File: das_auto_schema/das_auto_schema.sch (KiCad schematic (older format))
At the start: 0 parts

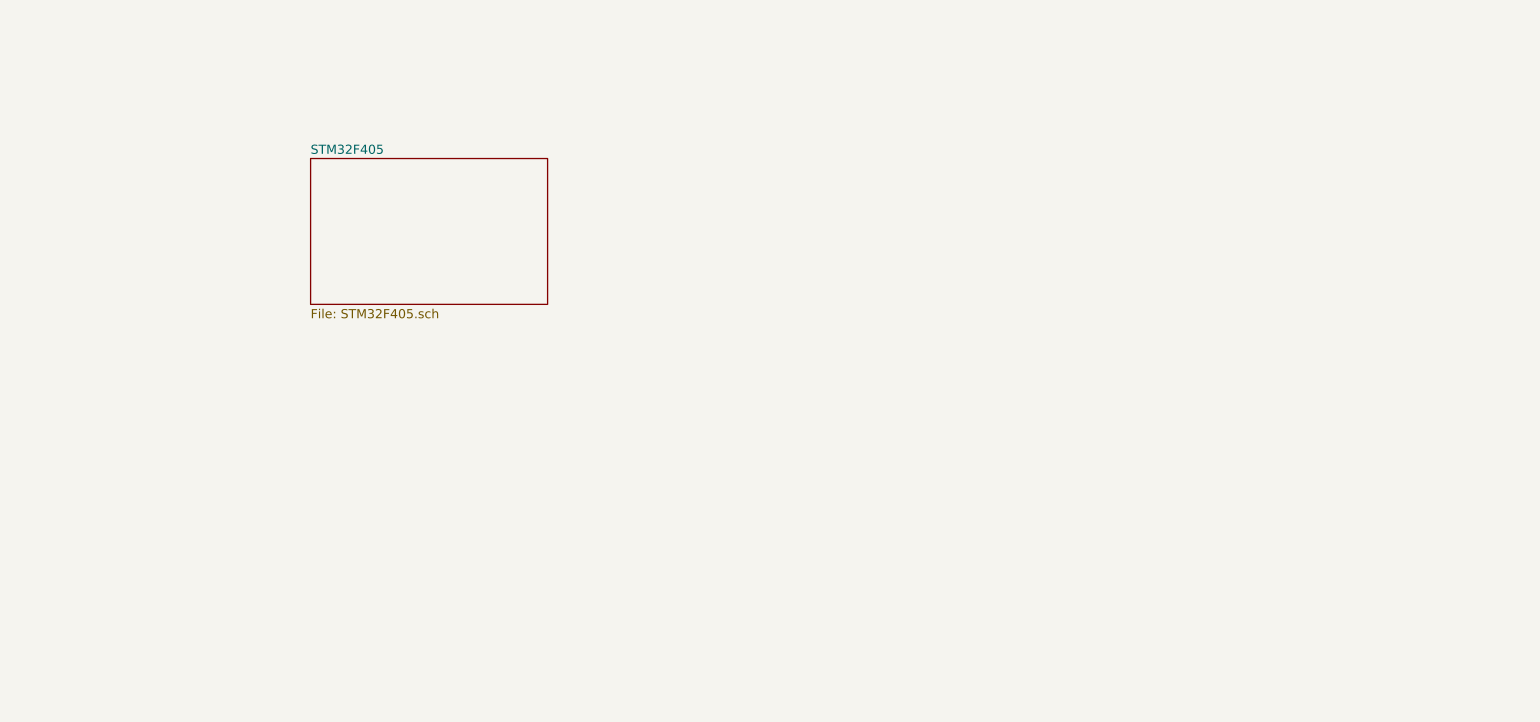
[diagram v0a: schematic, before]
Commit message: Added IMU + python script for realtime plot + Kicad updetes
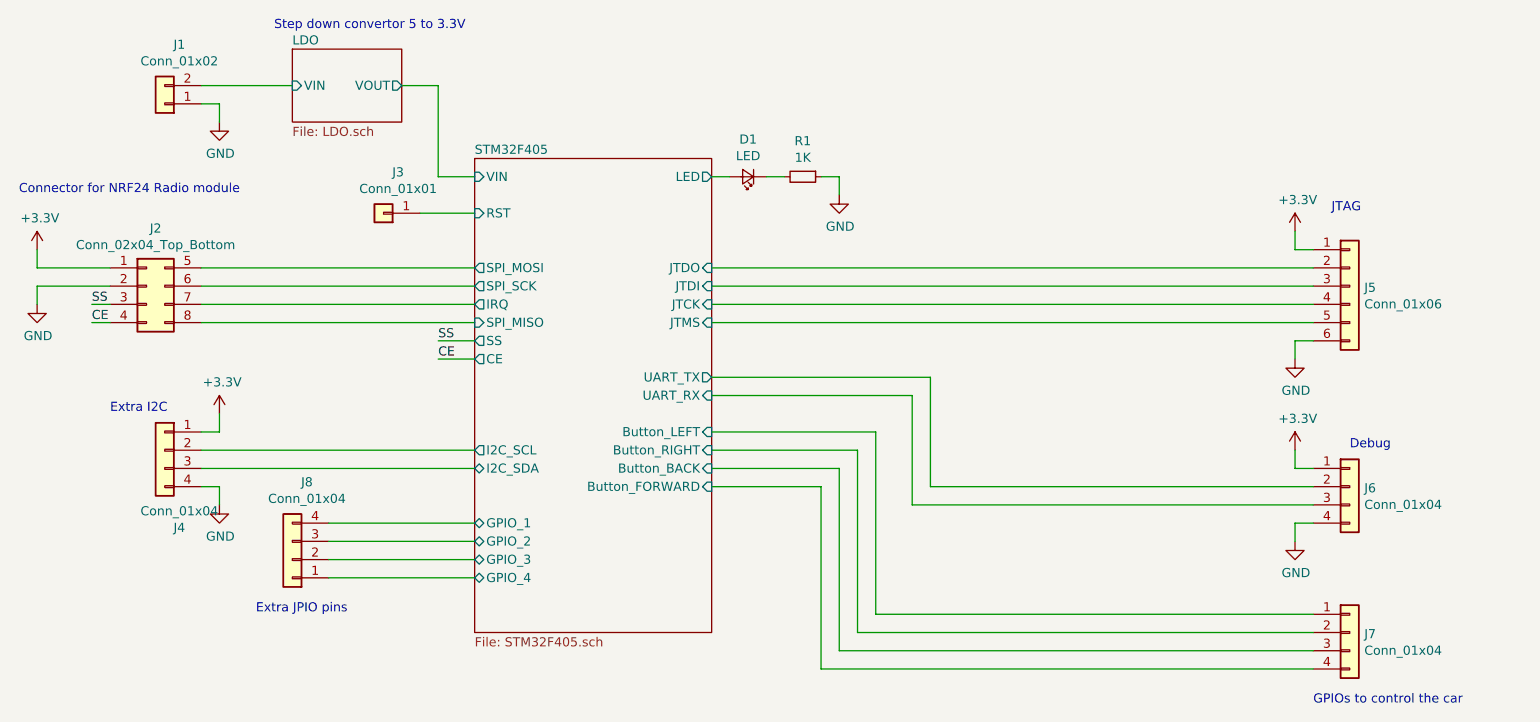
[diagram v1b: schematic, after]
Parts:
- added D1: LED, Resistor_SMD:R_1206_3216Metric, symbol Device:LED_Small
- added J1: Conn_01x02, Connector_PinSocket_2.54mm:PinSocket_1x02_P2.54mm_Vertical, symbol Connector_Generic:Conn_01x02
- added J2: Conn_02x04_Top_Bottom, Connector_PinSocket_2.54mm:PinSocket_2x04_P2.54mm_Vertical, symbol Connector_Generic:Conn_02x04_Top_Bottom
- added J3: Conn_01x01, Connector_PinSocket_2.54mm:PinSocket_1x01_P2.54mm_Vertical, symbol Connector_Generic:Conn_01x01
- added J4, J6, J7, J8: Conn_01x04, Connector_PinSocket_2.54mm:PinSocket_1x04_P2.54mm_Vertical, symbol Connector_Generic:Conn_01x04
- added J5: Conn_01x06, Connector_PinSocket_2.54mm:PinSocket_1x06_P2.54mm_Vertical, symbol Connector_Generic:Conn_01x06
- added R1: 1K, Resistor_SMD:R_0805_2012Metric, symbol Device:R_Small
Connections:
- new net: D1.1 (K), R1.2
- new net +3V3: J2.1 (Pin_1), J4.1 (Pin_1), J5.1 (Pin_1), J6.1 (Pin_1)
- new net CE: J2.4 (Pin_4)
- new net GND: J1.1 (Pin_1), J2.2 (Pin_2), J4.4 (Pin_4), J5.6 (Pin_6), J6.4 (Pin_4), R1.1
- new net LDO/VIN: J1.2 (Pin_2)
- new net SS: J2.3 (Pin_3)
- new net STM32F405/Button_BACK: J7.3 (Pin_3)
- new net STM32F405/Button_FORWARD: J7.4 (Pin_4)
- new net STM32F405/Button_LEFT: J7.1 (Pin_1)
- new net STM32F405/Button_RIGHT: J7.2 (Pin_2)
- new net STM32F405/GPIO_1: J8.4 (Pin_4)
- new net STM32F405/GPIO_2: J8.3 (Pin_3)
- new net STM32F405/GPIO_3: J8.2 (Pin_2)
- new net STM32F405/GPIO_4: J8.1 (Pin_1)
- new net STM32F405/I2C_SCL: J4.2 (Pin_2)
- new net STM32F405/I2C_SDA: J4.3 (Pin_3)
- new net STM32F405/IRQ: J2.7 (Pin_7)
- new net STM32F405/JTCK: J5.4 (Pin_4)
- new net STM32F405/JTDI: J5.3 (Pin_3)
- new net STM32F405/JTDO: J5.2 (Pin_2)
- new net STM32F405/JTMS: J5.5 (Pin_5)
- new net STM32F405/LED: D1.2 (A)
- new net STM32F405/RST: J3.1 (Pin_1)
- new net STM32F405/SPI_MISO: J2.8 (Pin_8)
- new net STM32F405/SPI_MOSI: J2.5 (Pin_5)
- new net STM32F405/SPI_SCK: J2.6 (Pin_6)
- new net STM32F405/UART_RX: J6.3 (Pin_3)
- new net STM32F405/UART_TX: J6.2 (Pin_2)
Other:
- note added: "Connector for NRF24 Radio module"
- note added: "Debug"
- note added: "Extra I2C"
- note added: "Extra JPIO pins"
- note added: "GPIOs to control the car"
- note added: "JTAG"
- note added: "Step down convertor 5 to 3.3V"
